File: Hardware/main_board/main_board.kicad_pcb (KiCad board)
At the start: 6 copper layers, 95.4 x 36.1 mm, 234 parts, among them J1 BATT, J2 LCD, J3 BACK_LIGHT, J4 SD, J5 NFC, J6 EXT1, J7 EXT0, J8 USB_C, Q1 DMN313DLT, SW1 OK, SW2 BACK, SW3 RIGHT, SW4 LEFT, SW5 UP, SW6 DOWN, T1 B0310J50100AHF, U1 STM32WB55RGVx, U10 BGS13S4N9E6327XTSA1, U11 NC7SZ32M5X, U12 LP5562TMX, U2 BQ27220YZFR, U3 BQ25896RTWR, U4 RS3221-3.3YF3, U5 LM66100DCK, U6 LM3281YFQR, U7 LM3281YFQR, U8 CC1101RGP, U9 BGS13S4N9E6327XTSA1, Y1 32MHz, Y2 32.768K, Y3 26MHz

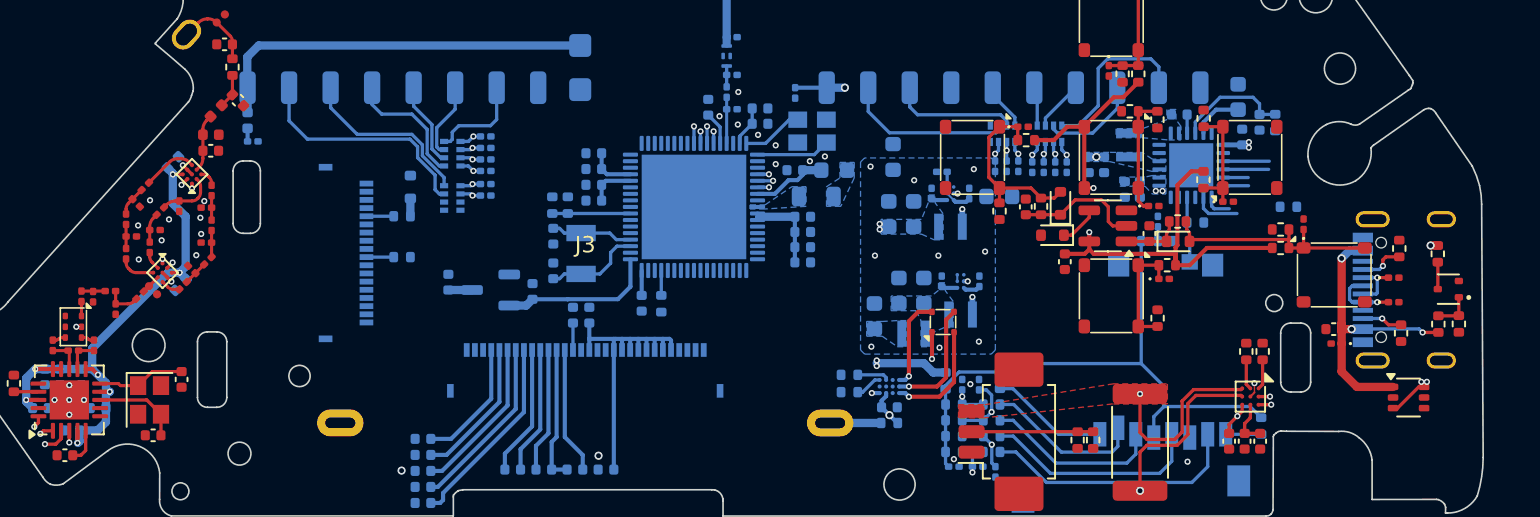
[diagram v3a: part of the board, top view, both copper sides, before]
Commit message: layout: routing peripherals
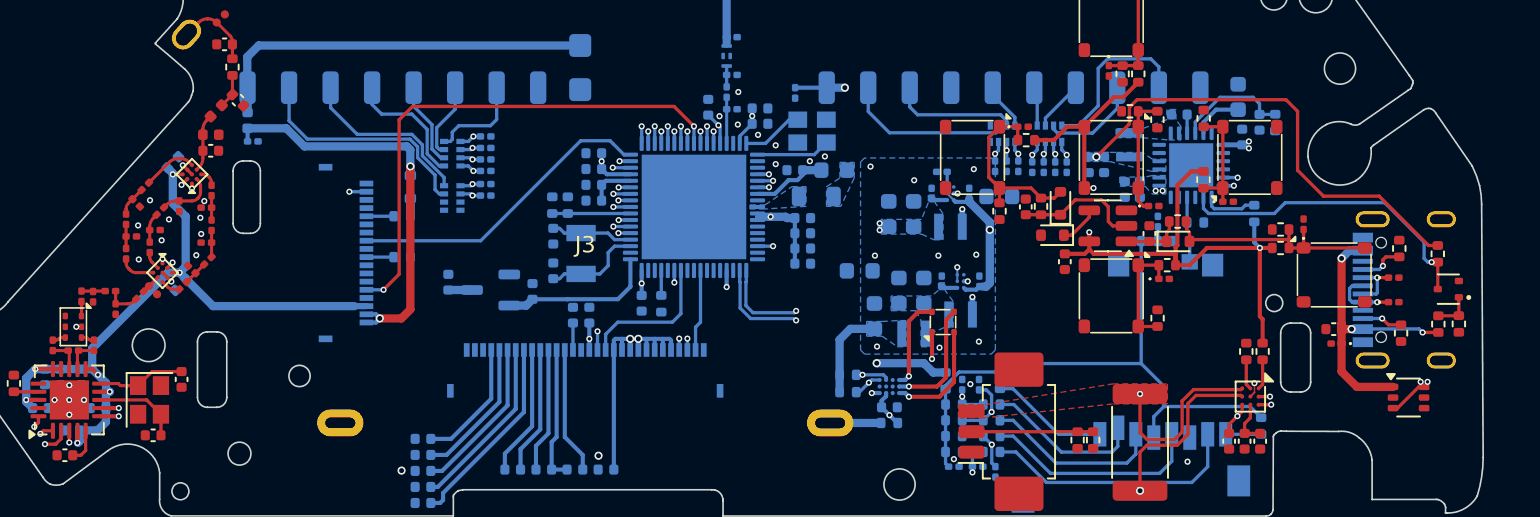
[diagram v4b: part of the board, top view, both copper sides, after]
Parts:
- moved FB1 7.26 mm to (163.8, 110.0), turned to 180 degrees
- moved R8 2.13 mm to (188.0, 106.5), turned to -90 degrees
- moved R6 0.09 mm to (163.1, 117.4)
- moved R7 0.09 mm to (163.1, 116.4)
- moved C1 0.08 mm to (160.4, 109.5)
- moved C4 0.08 mm to (160.4, 108.6)
- moved C7 0.08 mm to (160.4, 107.7)
- moved C8 0.08 mm to (160.4, 106.8)
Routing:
- net VUSB: track 27.8 -> 116.3 mm, vias 4 -> 6
- net /CC1101/CC1101_G0: track 0.00 -> 51.3 mm, vias 0 -> 2
- net /MCU/I2C_SCL: track 4.21 -> 51.1 mm, vias 1 -> 4
- net /MCU/I2C_SDA: track 3.89 -> 47.8 mm, vias 1 -> 3
- net /MCU/D+: track 4.00 -> 47.3 mm, vias 1 -> 2
- net /MCU/D-: track 3.41 -> 45.9 mm, vias 1 -> 2
- net /CC1101/RF_SW_0: track 5.79 -> 42.1 mm, vias 2 -> 3
- net +3.3V: track 105.3 -> 136.3 mm, vias 9 -> 19
- net /MCU/RFID_RF_IN: track 1.05 -> 31.8 mm, vias 1 -> 2
- net /MCU/IR_RX: track 0.00 -> 22.9 mm, vias 0 -> 2
- net /MCU/PB3: track 1.27 -> 20.7 mm, vias 1 -> 2
- net /MCU/PB2: track 2.00 -> 21.4 mm
- net /MCU/RFID_PULL: track 0.00 -> 19.0 mm
- net /MCU/PA7: track 1.27 -> 19.6 mm, vias 1 -> 2
- net /LCD/SPI_D_MOSI: track 4.10 -> 21.3 mm, vias 1 -> 3
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- added copper zone on In2.Cu, net +3.3V
- added copper zone on In2.Cu, net GND
- added copper zone on In3.Cu, net GND
